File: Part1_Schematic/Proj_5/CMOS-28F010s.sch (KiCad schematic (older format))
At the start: 5 parts, among them U12 28F010, U13 PAL16L8, U4 28F010

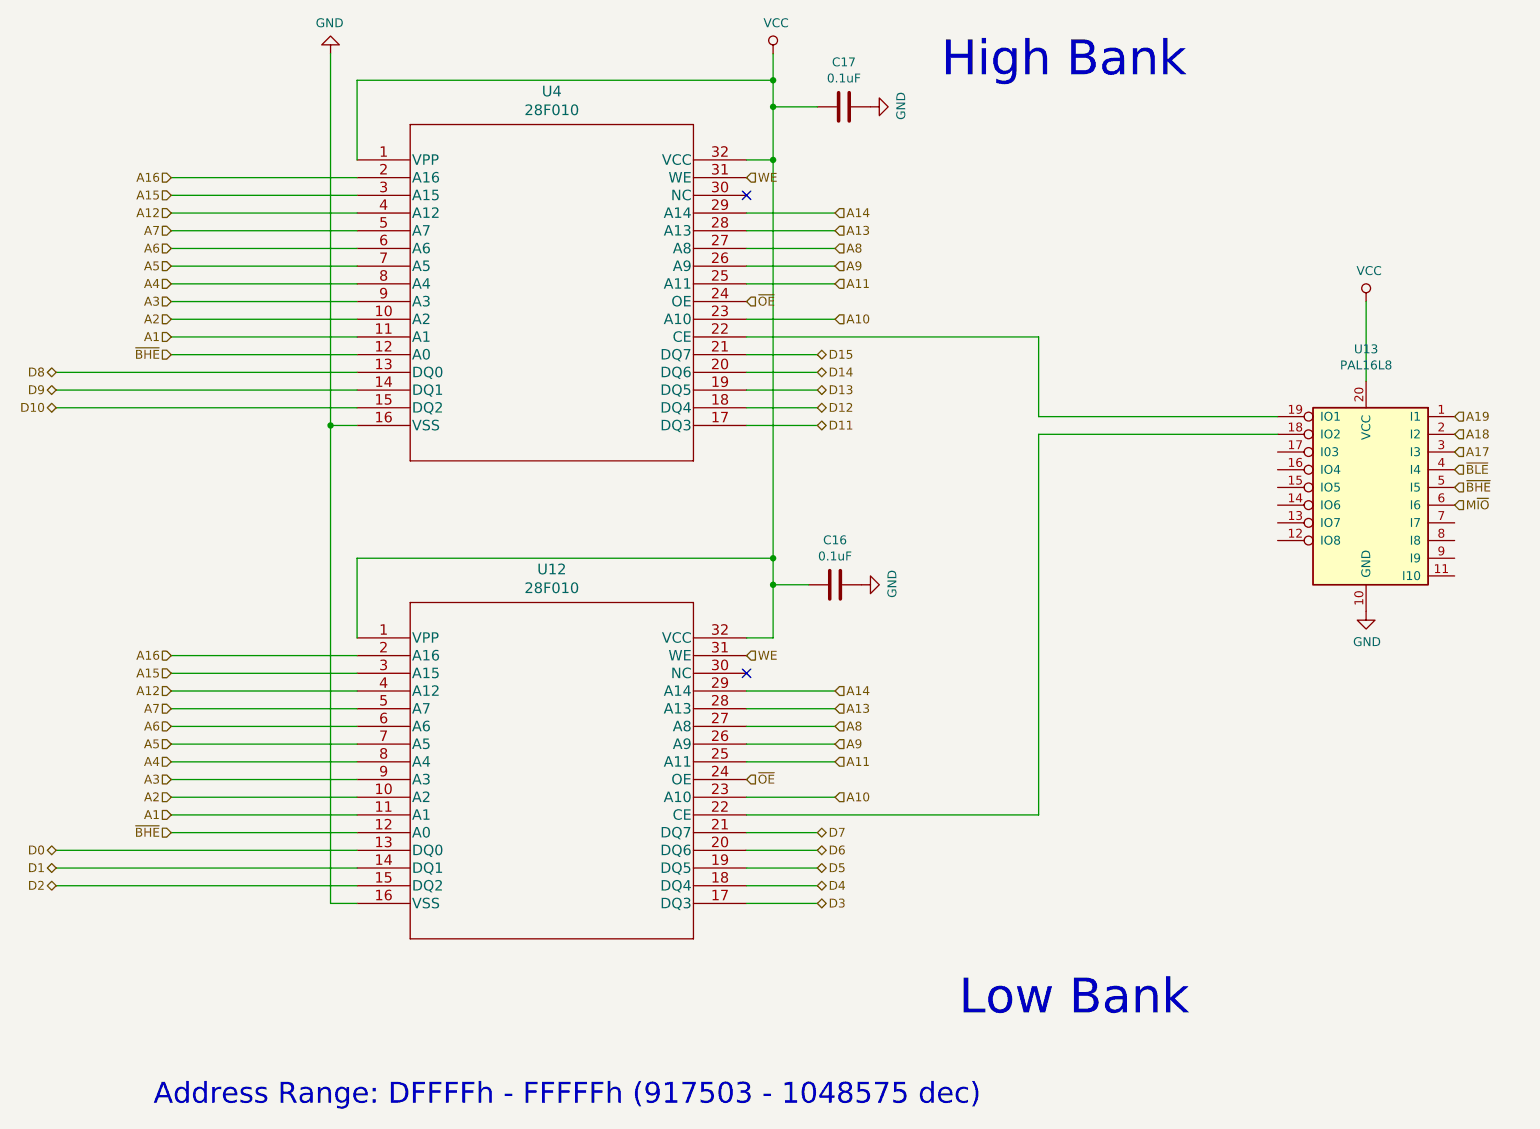
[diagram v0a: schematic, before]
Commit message: Addressing for 8279 and 8259
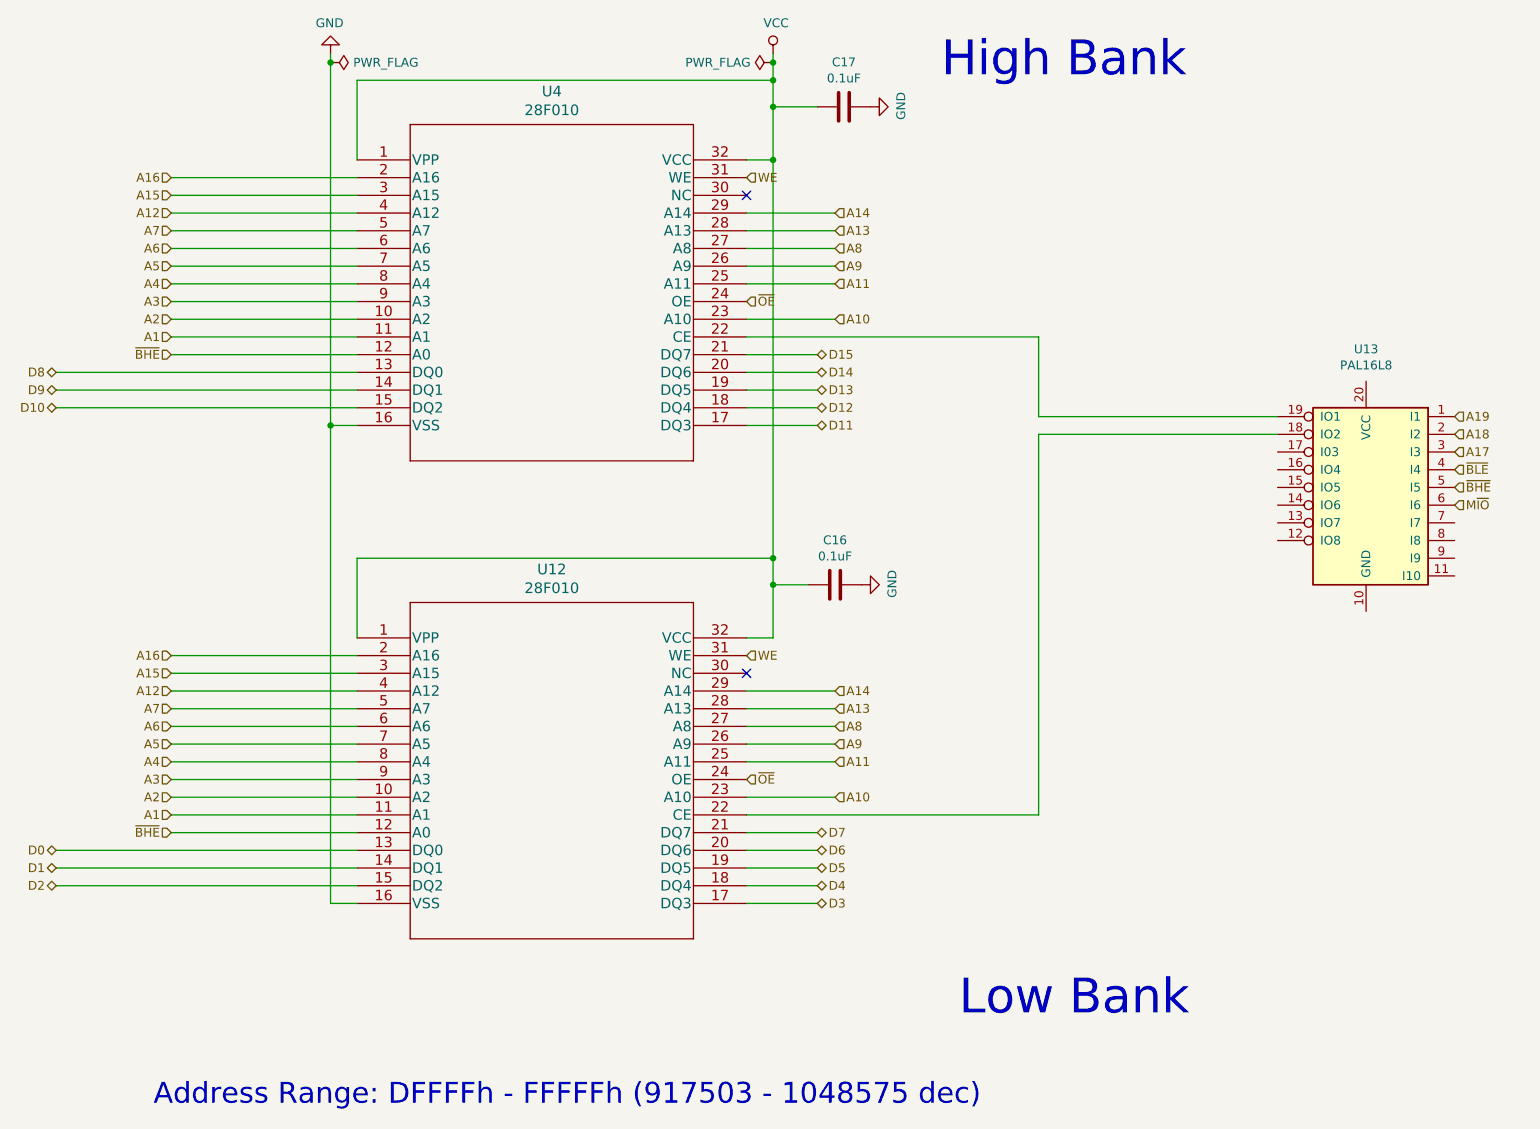
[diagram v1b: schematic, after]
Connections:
- net GND: no longer U13.10 (GND)
- net VCC: no longer U13.20 (VCC)
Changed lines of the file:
@@
 $Descr User 15748 23622
 encoding utf-8
-Sheet 4 10
+Sheet 5 9
 Title ""
 Date ""
@@
 	2950 4000 4650 4000
 Wire Wire Line
+	7000 2000 7000 2050
+Wire Wire Line
 	6850 2600 7000 2600
 $Comp
@@
 	-1   0    0    1
 $EndComp
+Wire Wire Line
+	4500 2000 4500 2050
 Wire Wire Line
 	4500 4100 4650 4100
@@
 	1    0    0    -1
 $EndComp
+$Comp
+L power:PWR_FLAG #FLG0103
+U 1 1 5EBED100
+P 4500 2050
+AR Path="/5EA045EA/5EBED100" Ref="#FLG0103"  Part="1"
+AR Path="/5EA98353/5EA34234/5EBED100" Ref="#FLG?"  Part="1"
+F 0 "#FLG0103" H 4500 2125 50  0001 C CNN
+F 1 "PWR_FLAG" V 4500 2178 50  0000 L CNN
+F 2 "" H 4500 2050 50  0001 C CNN
+F 3 "~" H 4500 2050 50  0001 C CNN
+	1    4500 2050
+	0    1    1    0
+$EndComp
+Connection ~ 4500 2050
+Wire Wire Line
+	4500 2050 4500 4100
+$Comp
+L power:PWR_FLAG #FLG0104
+U 1 1 5EBEE814
+P 7000 2050
+AR Path="/5EA045EA/5EBEE814" Ref="#FLG0104"  Part="1"
+AR Path="/5EA98353/5EA34234/5EBEE814" Ref="#FLG?"  Part="1"
+F 0 "#FLG0104" H 7000 2125 50  0001 C CNN
+F 1 "PWR_FLAG" V 7000 2177 50  0000 L CNN
+F 2 "" H 7000 2050 50  0001 C CNN
+F 3 "~" H 7000 2050 50  0001 C CNN
+	1    7000 2050
+	0    -1   -1   0
+$EndComp
 Wire Wire Line
 	7000 2150 4650 2150
@@
 Wire Wire Line
 	7000 2150 7000 2300
+Connection ~ 7000 2050
+Wire Wire Line
+	7000 2050 7000 2150
 Wire Wire Line
 	3600 5400 4650 5400
@@
 Text HLabel 10850 4550 2    50   Input ~ 0
 M~IO
-$Comp
-L power:GND #PWR047
-U 1 1 5F3A169C
-P 10350 5150
-AR Path="/5EA045EA/5F3A169C" Ref="#PWR047"  Part="1"
-AR Path="/5EA98353/5EA34234/5F3A169C" Ref="#PWR?"  Part="1"
-F 0 "#PWR047" H 10350 4900 50  0001 C CNN
-F 1 "GND" H 10355 4977 50  0000 C CNN
-F 2 "" H 10350 5150 50  0001 C CNN
-F 3 "" H 10350 5150 50  0001 C CNN
-	1    10350 5150
-	1    0    0    -1
-$EndComp
-$Comp
-L power:VCC #PWR046
-U 1 1 5F3AB457
-P 10350 3400
-AR Path="/5EA045EA/5F3AB457" Ref="#PWR046"  Part="1"
-AR Path="/5EA98353/5EA34234/5F3AB457" Ref="#PWR?"  Part="1"
-F 0 "#PWR046" H 10350 3250 50  0001 C CNN
-F 1 "VCC" H 10367 3573 50  0000 C CNN
-F 2 "" H 10350 3400 50  0001 C CNN
-F 3 "" H 10350 3400 50  0001 C CNN
-	1    10350 3400
-	1    0    0    -1
-$EndComp
-Wire Wire Line
-	10350 3400 10350 3850
-Wire Wire Line
-	4500 2000 4500 4100
-Wire Wire Line
-	7000 2000 7000 2150
 $EndSCHEMATC
